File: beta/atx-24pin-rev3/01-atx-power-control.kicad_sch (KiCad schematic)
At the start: 32 parts, among them J3 ATX-24 PSU, Q1 AO3400A, U4 74LVC1G17, U8 74LVC1G17

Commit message: Enforce readable BETA schematic layouts
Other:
- note added: "OUTPUT FORM (J4) = WORKING BASIS, not final. D-5a owner lean: very short captive stub + order-time optional extension (bundled SKU). Swappable section pending the formal form ruling -- see docs/standard- tier-review/ atx24-output-interface- panel-2026-07-03.md. J4 below stays the placeholder male Mini-Fit Jr header (locked spec Section 2.8) until that call."
- note removed: "OUTPUT FORM (J4) = WORKING BASIS, not final. D-5a owner lean: very short captive stub + order-time optional extension (bundled SKU). Swappable section pending the formal form ruling -- see docs/standard-tier-review/ atx24-output-interface-panel-2026-07-03.md. J4 below stays the placeholder male Mini-Fit Jr header (locked spec Section 2.8) until that call."

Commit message: Finalize compact Hub and ATX power-layout audit
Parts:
- J3: MPN (none) -> 39291247; Manufacturer (none) -> Molex; Note (none) -> 24-circuit Mini-Fit Jr right-angle through-hole ATX input h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
- J_SIG1: value SIG STUB 1x4 (mates db J20) -> SSQ-104-03-G-S; footprint cec-Connector_PinHeader_2.54mm:HDR-TH_4P-P2.54-V-M -> cec-Connector_PinSocket_2.54mm:PinSocket_1x04_P2.54mm_Vertical; MPN (none) -> SSQ-104-03-G-S; Manufacturer (none) -> Samtec; Note Owner ruling 2026-07-08 (closes output-daughterboard study 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 -> Vertical 1x4 socket; mates the daughterboard TSW-104-12-G-S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
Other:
- note removed: "ATX CONTROL-SIGNAL INTERACTION PS_ON#/PWR_OK/-12V (owner-approved 2026-07-14)"
- note removed: "ATX POWER PATH (interposer)"
- note removed: "H3a ferrite posture (owner addendum): USB D+/D- get NO series ferrite (SI killer) -- CMC only if a pre-scan ever demands it (H3a-d). FB2 is a 0R BRIDGE by default (bead position provisioned, populate on EMC evidence). CMC1 is DNP -- position reserved on CAN_H/CAN_L; a real DNP part will OPEN the bus unless the footprint/layout provides a jumper (layout-pass decision)."
- note removed: "OUTPUT FORM (J4) = WORKING BASIS, not final. D-5a owner lean: very short captive stub + order-time optional extension (bundled SKU). Swappable section pending the formal form ruling -- see docs/standard- tier-review/ atx24-output-interface- panel-2026-07-03.md. J4 below stays the placeholder male Mini-Fit Jr header (locked spec Section 2.8) until that call."

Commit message: pipeline: integrate route-aware physical design flow
Generalize critical-first placement and routing, future-congestion and power-authority planning, route provenance, process watchdogs, fab/thermal validation, dashboard review, and XFCN integration. Add the supporting board contracts, component libraries, documentation, and regression coverage.
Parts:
- removed TB10, TB3, TB7, TB8: TE 63969-1, cec-Connector_Blade:TE_63969_FASTON_Receptacle_250_Vertical_THT, symbol cec-vendor:Keystone_3586_Blade_Clip
- J_SIG1: value SSQ-104-03-G-S -> SSQ-102-03-G-D; footprint cec-Connector_PinSocket_2.54mm:PinSocket_1x04_P2.54mm_Vertical -> cec-Connector_PinSocket_2.54mm:Samtec_SSQ-102-03-G-D_2x02_P2.54mm_Vertical; MPN SSQ-104-03-G-S -> SSQ-102-03-G-D; Note Vertical 1x4 socket; mates the daughterboard TSW-104-12-G-S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 -> Mates TSW-102-16-G-D-RA; 1=-12V, 2=PS_ON#, 3=PWR_OK, 4=GND.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
- TB1: value TE 63969-1 -> XFCN T34069; footprint cec-Connector_Blade:TE_63969_FASTON_Receptacle_250_Vertical_THT -> cec-Connector_Screw:XFCN_T34069_THT_M3_40A; symbol cec-vendor:Keystone_3586_Blade_Clip -> cec-Connector_Screw:XFCN_T34069; CAD Status (none) -> LCSC/EasyEDA footprint and native 3D model; sample verifica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; Current Rating (none) -> 40 A manufacturer-stated; qualification required; Integration Note (none) -> Prototype XFCN interface; TE blade architecture remains the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; JLC Library (none) -> Extended; manualWeld / Wave Soldering; LCSC C2961150 -> C481452; MPN 63969-1 -> T34069; Manufacturer TE Connectivity -> XFCN; Note Output daughterboard blade clip, ratified joint 12V (spec S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 -> (none); Source Drawing (none) -> lib/datasheets/XFCN_T34069_C481452.pdf; Thread Torque (none) -> 0.5 N*m
- TB2: value TE 63969-1 -> XFCN T34069; footprint cec-Connector_Blade:TE_63969_FASTON_Receptacle_250_Vertical_THT -> cec-Connector_Screw:XFCN_T34069_THT_M3_40A; symbol cec-vendor:Keystone_3586_Blade_Clip -> cec-Connector_Screw:XFCN_T34069; CAD Status (none) -> LCSC/EasyEDA footprint and native 3D model; sample verifica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; Current Rating (none) -> 40 A manufacturer-stated; qualification required; Integration Note (none) -> Prototype XFCN interface; TE blade architecture remains the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; JLC Library (none) -> Extended; manualWeld / Wave Soldering; LCSC C2961150 -> C481452; MPN 63969-1 -> T34069; Manufacturer TE Connectivity -> XFCN; Note Output daughterboard blade clip, ratified joint 5V (1 of 2)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 -> (none); Source Drawing (none) -> lib/datasheets/XFCN_T34069_C481452.pdf; Thread Torque (none) -> 0.5 N*m
- TB4: value TE 63969-1 -> XFCN T34069; footprint cec-Connector_Blade:TE_63969_FASTON_Receptacle_250_Vertical_THT -> cec-Connector_Screw:XFCN_T34069_THT_M3_40A; symbol cec-vendor:Keystone_3586_Blade_Clip -> cec-Connector_Screw:XFCN_T34069; CAD Status (none) -> LCSC/EasyEDA footprint and native 3D model; sample verifica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; Current Rating (none) -> 40 A manufacturer-stated; qualification required; Integration Note (none) -> Prototype XFCN interface; TE blade architecture remains the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; JLC Library (none) -> Extended; manualWeld / Wave Soldering; LCSC C2961150 -> C481452; MPN 63969-1 -> T34069; Manufacturer TE Connectivity -> XFCN; Note Output daughterboard blade clip, ratified joint 3.3V (spec 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 -> (none); Source Drawing (none) -> lib/datasheets/XFCN_T34069_C481452.pdf; Thread Torque (none) -> 0.5 N*m
- TB5: value TE 63969-1 -> XFCN T34069; footprint cec-Connector_Blade:TE_63969_FASTON_Receptacle_250_Vertical_THT -> cec-Connector_Screw:XFCN_T34069_THT_M3_40A; symbol cec-vendor:Keystone_3586_Blade_Clip -> cec-Connector_Screw:XFCN_T34069; CAD Status (none) -> LCSC/EasyEDA footprint and native 3D model; sample verifica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; Current Rating (none) -> 40 A manufacturer-stated; qualification required; Integration Note (none) -> Prototype XFCN interface; TE blade architecture remains the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; JLC Library (none) -> Extended; manualWeld / Wave Soldering; LCSC C2961150 -> C481452; MPN 63969-1 -> T34069; Manufacturer TE Connectivity -> XFCN; Note Output daughterboard blade clip, ratified joint 5VSB (spec 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 -> (none); Source Drawing (none) -> lib/datasheets/XFCN_T34069_C481452.pdf; Thread Torque (none) -> 0.5 N*m
- TB6: value TE 63969-1 -> TTR32100127-0600; footprint cec-Connector_Blade:TE_63969_FASTON_Receptacle_250_Vertical_THT -> cec-Connector_Screw:XFCN_TTR32100127-0600_THT_M3_60A; symbol cec-vendor:Keystone_3586_Blade_Clip -> cec-Connector_Screw:XFCN_TTR32100127-0600; CAD Status (none) -> LCSC/EasyEDA footprint; project-authored datasheet-envelope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; Current Rating (none) -> 60 A manufacturer-stated; qualification required; Integration Note (none) -> Prototype XFCN interface; TE blade architecture remains the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; JLC Library (none) -> Extended; manualWeld / Wave Soldering; LCSC C2961150 -> C45384691; MPN 63969-1 -> TTR32100127-0600; Manufacturer TE Connectivity -> XFCN; Note Output daughterboard blade clip, ratified joint GND (1 of 4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 -> (none); Source Drawing (none) -> lib/datasheets/XFCN_TTR32100127-0600_C45384691.pdf; Thread Torque (none) -> 1.0 N*m
- TB9: value TE 63969-1 -> TTR32100127-0600; footprint cec-Connector_Blade:TE_63969_FASTON_Receptacle_250_Vertical_THT -> cec-Connector_Screw:XFCN_TTR32100127-0600_THT_M3_60A; symbol cec-vendor:Keystone_3586_Blade_Clip -> cec-Connector_Screw:XFCN_TTR32100127-0600; CAD Status (none) -> LCSC/EasyEDA footprint; project-authored datasheet-envelope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; Current Rating (none) -> 60 A manufacturer-stated; qualification required; Integration Note (none) -> Prototype XFCN interface; TE blade architecture remains the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; JLC Library (none) -> Extended; manualWeld / Wave Soldering; LCSC C2961150 -> C45384691; MPN 63969-1 -> TTR32100127-0600; Manufacturer TE Connectivity -> XFCN; Note Output daughterboard blade clip, ratified joint GND (4 of 4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 -> (none); Source Drawing (none) -> lib/datasheets/XFCN_TTR32100127-0600_C45384691.pdf; Thread Torque (none) -> 1.0 N*m

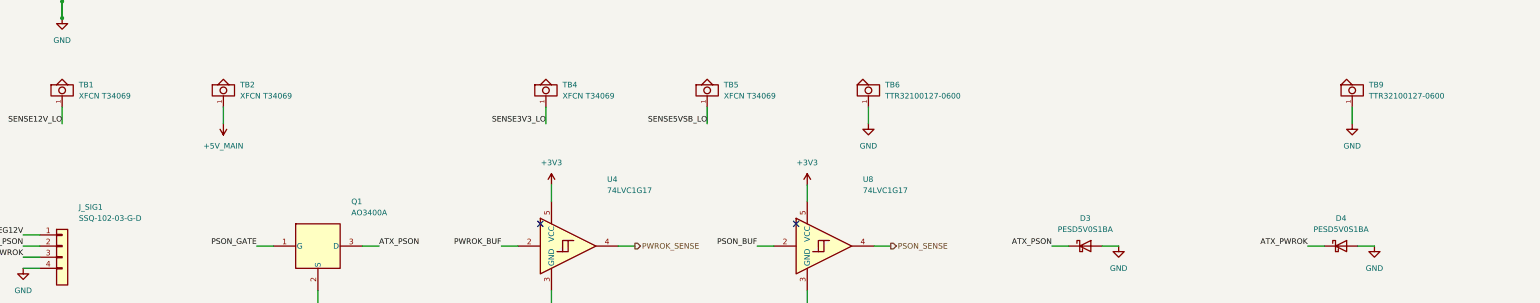
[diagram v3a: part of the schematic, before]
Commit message: Generalize route-aware PCB placement pipeline
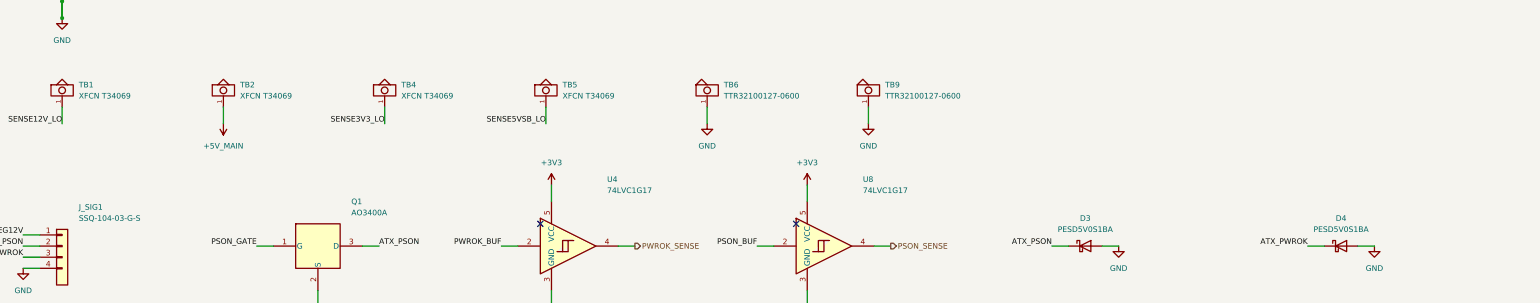
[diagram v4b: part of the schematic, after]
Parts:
- J_SIG1: value SSQ-102-03-G-D -> SSQ-104-03-G-S; footprint cec-Connector_PinSocket_2.54mm:Samtec_SSQ-102-03-G-D_2x02_P2.54mm_Vertical -> cec-Connector_PinSocket_2.54mm:PinSocket_1x04_P2.54mm_Vertical; MPN SSQ-102-03-G-D -> SSQ-104-03-G-S; Note Mates TSW-102-16-G-D-RA; 1=-12V, 2=PS_ON#, 3=PWR_OK, 4=GND.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 -> Vertical 1x4 socket; mates the daughterboard TSW-104-12-G-S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

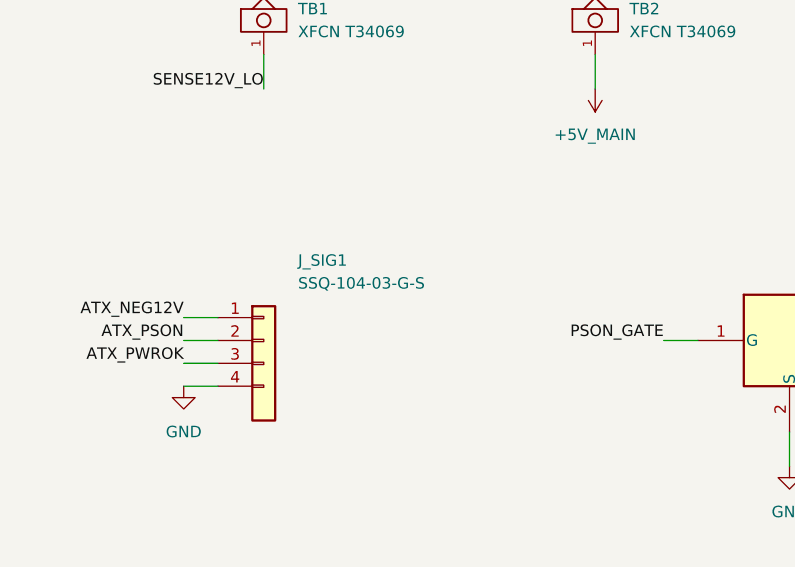
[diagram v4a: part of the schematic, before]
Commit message: Keep qualified interface copper inside board
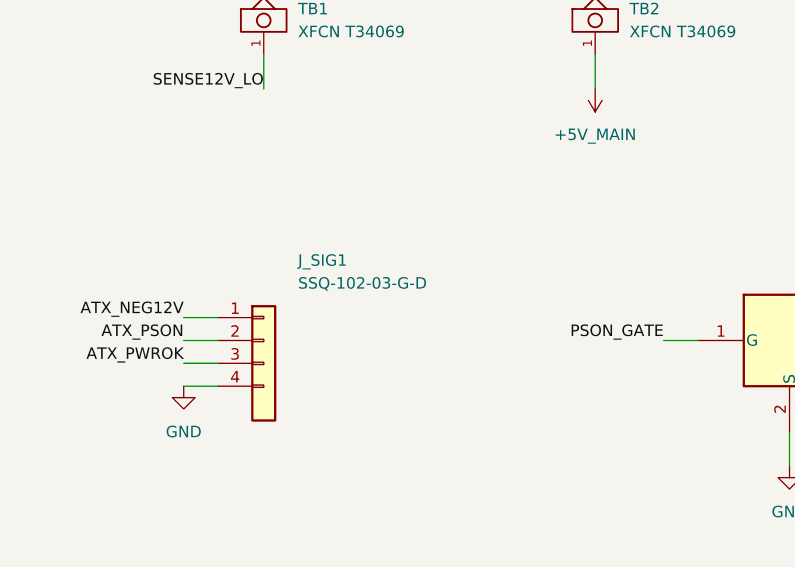
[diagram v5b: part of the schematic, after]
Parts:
- J_SIG1: value SSQ-104-03-G-S -> SSQ-102-03-G-D; footprint cec-Connector_PinSocket_2.54mm:PinSocket_1x04_P2.54mm_Vertical -> cec-Connector_PinSocket_2.54mm:Samtec_SSQ-102-03-G-D_2x02_P2.54mm_Vertical; MPN SSQ-104-03-G-S -> SSQ-102-03-G-D; Note Vertical 1x4 socket; mates the daughterboard TSW-104-12-G-S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 -> Mates TSW-102-16-G-D-RA; 1=-12V, 2=PS_ON#, 3=PWR_OK, 4=GND.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
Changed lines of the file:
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@@
 		(fields_autoplaced yes)
 		(property "Reference" "J_SIG1" (at 43.18 153.67 0) (effects (font (size 1.27 1.27)) (justify left)))
-		(property "Value" "SSQ-104-03-G-S" (at 43.18 156.21 0) (effects (font (size 1.27 1.27)) (justify left)))
-		(property "Footprint" "cec-Connector_PinSocket_2.54mm:PinSocket_1x04_P2.54mm_Vertical" (at 39.37 162.56 0) (effects (font (size 1.27 1.27)) (hide yes)))
-		(property "Datasheet" "https://www.samtec.com/products/ssq-104-03-g-s" (at 39.37 162.56 0) (effects (font (size 1.27 1.27)) (hide yes)))
-		(property "Note" "Vertical 1x4 socket; mates the daughterboard TSW-104-12-G-S-RA long-tail right-angle header pin-for-pin." (at 39.37 162.56 0) (effects (font (size 1.27 1.27)) (hide yes)))
+		(property "Value" "SSQ-102-03-G-D" (at 43.18 156.21 0) (effects (font (size 1.27 1.27)) (justify left)))
+		(property "Footprint" "cec-Connector_PinSocket_2.54mm:Samtec_SSQ-102-03-G-D_2x02_P2.54mm_Vertical" (at 39.37 162.56 0) (effects (font (size 1.27 1.27)) (hide yes)))
+		(property "Datasheet" "https://suddendocs.samtec.com/prints/ssq-1xx-xx-xxx-x-xx-xxx-xx-x-mkt.pdf" (at 39.37 162.56 0) (effects (font (size 1.27 1.27)) (hide yes)))
+		(property "Note" "Mates TSW-102-16-G-D-RA; 1=-12V, 2=PS_ON#, 3=PWR_OK, 4=GND. First-article mated-transform and engagement check required." (at 39.37 162.56 0) (effects (font (size 1.27 1.27)) (hide yes)))
 		(property "Manufacturer" "Samtec" (at 39.37 162.56 0) (effects (font (size 1.27 1.27)) (hide yes)))
-		(property "MPN" "SSQ-104-03-G-S" (at 39.37 162.56 0) (effects (font (size 1.27 1.27)) (hide yes)))
+		(property "MPN" "SSQ-102-03-G-D" (at 39.37 162.56 0) (effects (font (size 1.27 1.27)) (hide yes)))
 		(property "Description" "2x2 2.54 mm vertical female socket, 8.51 mm body and 10.01 mm lead-style -03 tail; double-row odd/even-by-column pin geometry." (at 39.37 162.56 0) (effects (font (size 1.27 1.27)) (hide yes)))
 		(pin "1")
